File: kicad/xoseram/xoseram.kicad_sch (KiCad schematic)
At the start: 0 parts

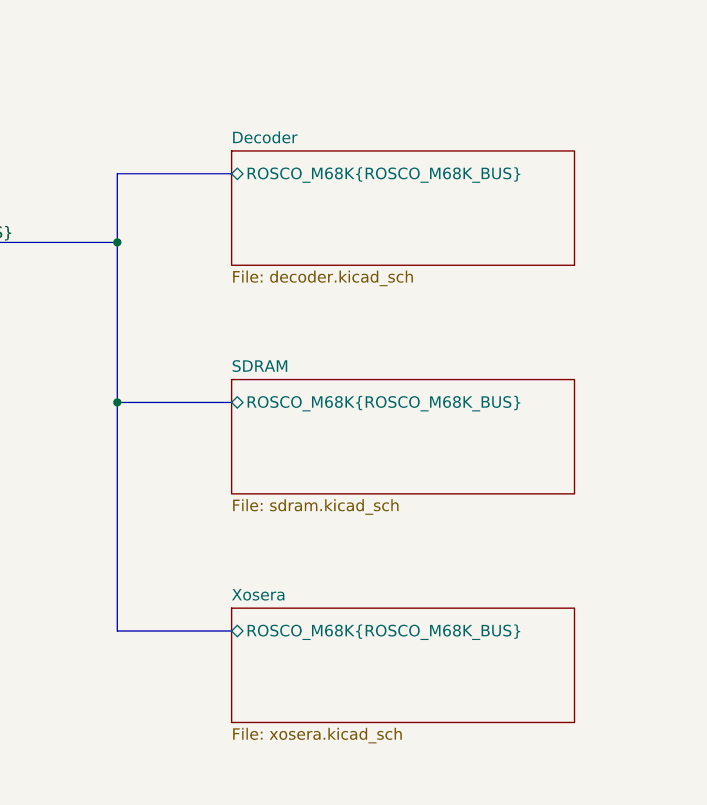
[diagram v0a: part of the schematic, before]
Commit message: Rename ROSCO_M68K_BUS for clarity
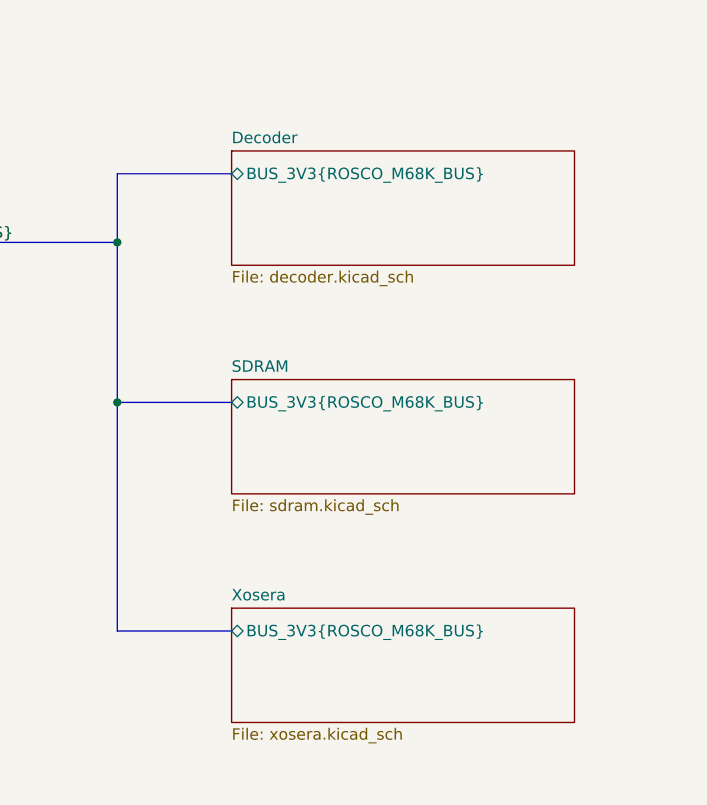
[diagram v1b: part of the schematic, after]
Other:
- sheet Decoder ports: added BUS_3V3{ROSCO_M68K_BUS}; removed ROSCO_M68K{ROSCO_M68K_BUS}
- sheet SDRAM ports: added BUS_3V3{ROSCO_M68K_BUS}; removed ROSCO_M68K{ROSCO_M68K_BUS}
- sheet Xosera ports: added BUS_3V3{ROSCO_M68K_BUS}; removed ROSCO_M68K{ROSCO_M68K_BUS}
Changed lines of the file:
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@@
 			)
 		)
-		(pin "ROSCO_M68K{ROSCO_M68K_BUS}" bidirectional
+		(pin "BUS_3V3{ROSCO_M68K_BUS}" bidirectional
 			(at 215.9 66.04 180)
 			(effects
@@
 			)
 		)
-		(pin "ROSCO_M68K{ROSCO_M68K_BUS}" bidirectional
+		(pin "BUS_3V3{ROSCO_M68K_BUS}" bidirectional
 			(at 215.9 91.44 180)
 			(effects
@@
 			)
 		)
-		(pin "ROSCO_M68K{ROSCO_M68K_BUS}" bidirectional
+		(pin "BUS_3V3{ROSCO_M68K_BUS}" bidirectional
 			(at 215.9 40.64 180)
 			(effects

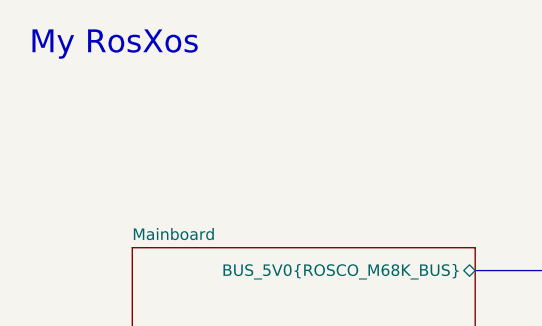
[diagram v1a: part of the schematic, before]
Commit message: Make DVI BSEL high for 24-bit mode
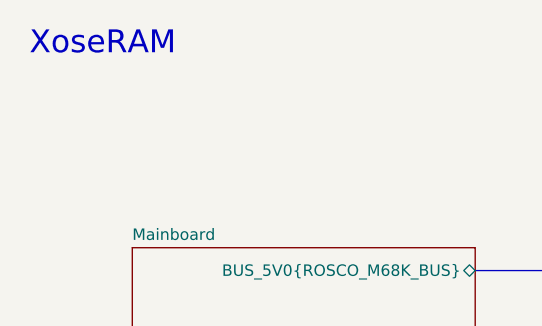
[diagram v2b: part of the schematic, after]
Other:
- note added: "${TITLE}"
- note removed: "My RosXos"
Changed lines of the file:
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@@
 		)
 	)
-	(text "My RosXos"
+	(text "${TITLE}"
 		(exclude_from_sim no)
 		(at 13.97 13.97 0)

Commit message: Update dates and license art
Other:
- company: 0xTJ -> Thomas Jager
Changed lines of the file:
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@@
 	(title_block
 		(title "XoseRAM")
-		(date "2024-05-08")
+		(date "2024-05-09")
 		(rev "A")
-		(company "0xTJ")
+		(company "Thomas Jager")
+		(comment 1 "Licensed under CERN OHL v.1.2")
 	)
 	(junction
